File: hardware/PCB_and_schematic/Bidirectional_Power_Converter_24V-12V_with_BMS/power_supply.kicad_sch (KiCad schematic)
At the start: 0 parts

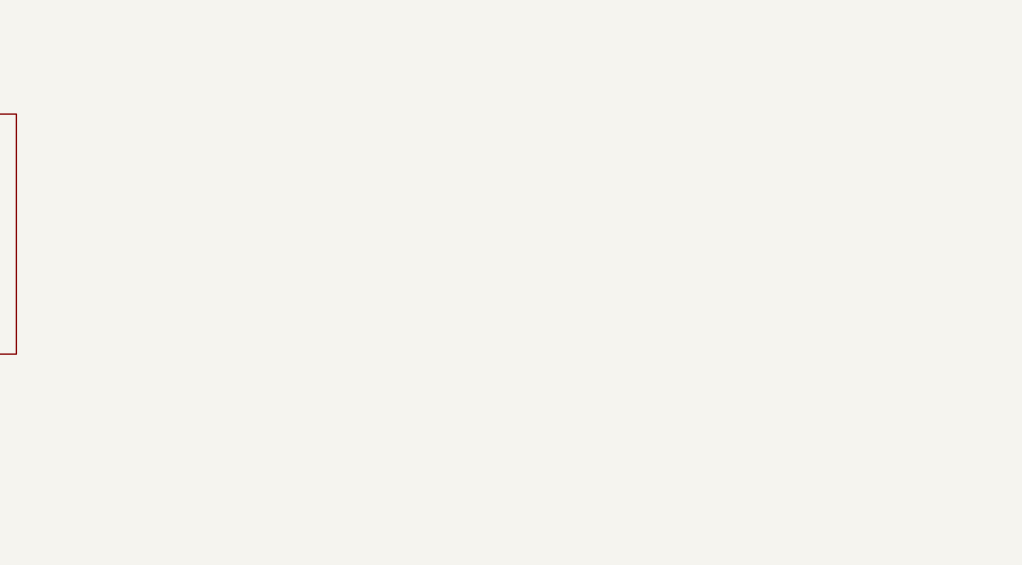
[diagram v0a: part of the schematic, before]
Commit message: Drawning schematic for buck/boost converter
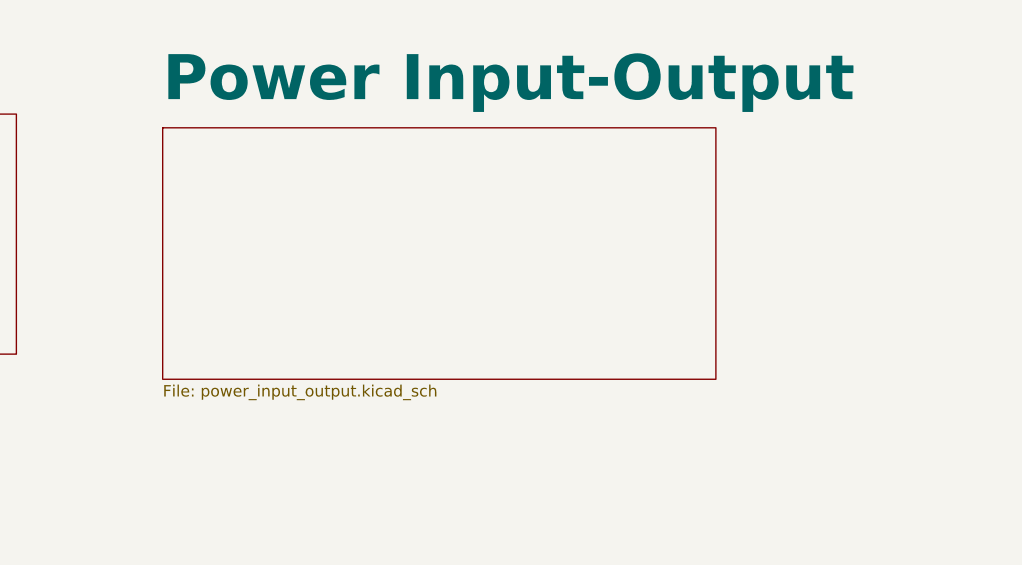
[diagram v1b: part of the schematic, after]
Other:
- added sheet Power Input-Output (power_input_output.kicad_sch)
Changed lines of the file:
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@@
+	)
+	(sheet
+		(at 212.09 24.13)
+		(size 61.468 27.94)
+		(fields_autoplaced yes)
+		(stroke
+			(width 0.1524)
+			(type solid)
+		)
+		(fill
+			(color 0 0 0 0.0000)
+		)
+		(property "Sheetname" "Power Input-Output"
+			(at 212.09 21.5534 0)
+			(effects
+				(font
+					(size 5 5)
+					(bold yes)
+				)
+				(justify left bottom)
+			)
+		)
+		(property "Sheetfile" "power_input_output.kicad_sch"
+			(at 212.09 52.6546 0)
+			(effects
+				(font
+					(size 1.27 1.27)
+				)
+				(justify left top)
+			)
+		)
+		(instances
+			(project "Bidirectional_Power_Converter_24V-12V_with_BMS"
+				(path "/57ff2453-26d1-489b-aa83-9af273df178f/81802b0c-d137-483c-9072-3d8784bb4773"
+					(page "2")
+				)
+			)
+		)
 	)
 	(sheet

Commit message: buck-boost conv update
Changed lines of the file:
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@@
 	(paper "A4")
 	(sheet
-		(at 50.038 24.384)
+		(at 39.878 40.894)
 		(size 61.468 27.94)
 		(fields_autoplaced yes)
@@
 		)
 		(property "Sheetname" "Boost Converter"
-			(at 50.038 21.8074 0)
+			(at 39.878 38.3174 0)
 			(effects
 				(font
@@
 		)
 		(property "Sheetfile" "boost.kicad_sch"
-			(at 50.038 52.9086 0)
+			(at 39.878 69.4186 0)
 			(effects
 				(font
@@
 	)
 	(sheet
-		(at 212.09 24.13)
+		(at 201.93 40.64)
 		(size 61.468 27.94)
 		(fields_autoplaced yes)
@@
 		)
 		(property "Sheetname" "Power Input-Output"
-			(at 212.09 21.5534 0)
+			(at 201.93 38.0634 0)
 			(effects
 				(font
@@
 		)
 		(property "Sheetfile" "power_input_output.kicad_sch"
-			(at 212.09 52.6546 0)
+			(at 201.93 69.1646 0)
 			(effects
 				(font
@@
 	)
 	(sheet
-		(at 134.112 22.606)
+		(at 123.952 39.116)
 		(size 61.722 26.67)
 		(fields_autoplaced yes)
@@
 		)
 		(property "Sheetname" "Buck Converter"
-			(at 134.112 20.0294 0)
+			(at 123.952 36.5394 0)
 			(effects
 				(font
@@
 		)
 		(property "Sheetfile" "buck.kicad_sch"
-			(at 134.112 49.8606 0)
+			(at 123.952 66.3706 0)
 			(effects
 				(font
@@
 	)
 	(sheet
-		(at 53.086 86.868)
+		(at 40.386 89.408)
 		(size 59.182 30.48)
 		(fields_autoplaced yes)
@@
 		)
 		(property "Sheetname" "Microcontroller"
-			(at 53.086 84.2914 0)
+			(at 40.386 86.8314 0)
 			(effects
 				(font
@@
 		)
 		(property "Sheetfile" "microcontroller.kicad_sch"
-			(at 53.086 117.9326 0)
+			(at 40.386 120.4726 0)
 			(effects
 				(font
